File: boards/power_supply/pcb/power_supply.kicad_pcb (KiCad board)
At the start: 2 copper layers, 258 x 170 mm, 227 parts, among them J101 Battery, J102 5V, J103 3.3V, J104 V_ISOLATED, J201 Conn_01x04_Socket, J202 12401826E412A, J203 USB IDC, J301 Conn_01x02_Socket, J302 Conn_01x04_Socket, SW201 PTS526 SK15 SMTR2 LFS, T701 150u, U201 USBLC6-2P6

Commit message: initial psu charger layout
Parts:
- J101: footprint Connector_AMASS:AMASS_XT30U-F_1x02_P5.0mm_Vertical -> xt30:AMASS_XT30U-F_1x02_P5.0mm_Vertical
- J102, J103, J104, J301: footprint Connector_PinHeader_2.54mm:PinHeader_1x02_P2.54mm_Vertical -> Connector_JST:JST_XH_B2B-XH-A_1x02_P2.50mm_Vertical
- J202: value 12401826E412A -> USB4105-GF-A; footprint 12401826E412A:12401826E412A -> USB4105-GF-A:USB4105-GF-A
- J302: footprint Connector_PinHeader_2.54mm:PinHeader_1x04_P2.54mm_Vertical -> Connector_JST:JST_XH_B4B-XH-A_1x04_P2.50mm_Vertical
- moved JP301 73.1 mm to (106.9, 155.2), turned to 90 degrees
- moved R304 72.3 mm to (104.4, 152.1), turned to -90 degrees
- moved JP304 70.6 mm to (91.9, 155.2), turned to 90 degrees
- moved JP305 68.2 mm to (104.4, 155.2), turned to 90 degrees
- moved JP302 68.0 mm to (99.4, 155.2), turned to 90 degrees
- moved R305 67.7 mm to (96.9, 152.1), turned to -90 degrees
- moved JP308 67.3 mm to (101.9, 155.2), turned to 90 degrees
- moved J301 66.2 mm to (85.0, 150.4), turned to 90 degrees
- moved R301 65.8 mm to (106.9, 152.1), turned to -90 degrees
- moved R307 64.4 mm to (101.9, 152.1), turned to -90 degrees
- moved JP310 64.3 mm to (99.4, 148.9), turned to 90 degrees
- moved JP307 64.3 mm to (96.9, 148.9), turned to 90 degrees
- moved JP306 63.7 mm to (96.9, 155.2), turned to 90 degrees
- moved R214 63.6 mm to (111.1, 154.5), turned to -90 degrees
- moved JP309 63.5 mm to (94.4, 155.2), turned to 90 degrees
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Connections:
- D201 pad 2: /USB-C PD/VBUS -> VBUS
- D205 pad 2: /USB-C PD/VBUS -> VBUS
- J101 pad 1: /Charger/VBATT -> GND
- J101 pad 2: GND -> /Charger/VBATT
- R206 pad 1: /USB-C PD/VBUS -> VBUS
- U203 pad 5: /USB-C PD/VBUS -> VBUS
- U203 pad 6: /USB-C PD/VBUS -> VBUS
- U203 pad 7: /USB-C PD/VBUS -> VBUS
- U203 pad 8: /USB-C PD/VBUS -> VBUS
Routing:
- net /Charger/ILIM: track 0.00 -> 31.0 mm, vias 0 -> 2
- net VBUS: track 0.00 -> 25.9 mm
- net /Charger/CELL: track 0.00 -> 19.0 mm, vias 0 -> 2
- net /USB-C PD/CC1: track 0.00 -> 18.2 mm
- net /USB-C PD/CC2: track 0.00 -> 17.8 mm
- net /Charger/NTC: track 0.00 -> 17.8 mm, vias 0 -> 2
- net /Charger/ISET: track 0.00 -> 15.9 mm, vias 0 -> 2
- net /Charger/VB: track 0.00 -> 15.5 mm, vias 0 -> 2
- net /USB-C PD/ADDR1: track 0.00 -> 12.4 mm
- net /USB-C PD/ADDR0: track 0.00 -> 11.1 mm
- net Net-(U301-VCC): track 0.00 -> 9.58 mm, vias 0 -> 2
- net Net-(U301-CSP): track 0.00 -> 9.36 mm, vias 0 -> 2
- net Net-(C202-Pad1): track 0.00 -> 8.00 mm
- net Net-(U301-BST): track 0.00 -> 7.61 mm, vias 0 -> 2
- net /Charger/VIN: track 0.00 -> 7.54 mm
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- added copper zone on F.Cu, net /Buck-Boost-1/VIN
- added copper zone on F.Cu, net /Charger/VBATT
- added copper zone on F.Cu, net /Charger/VIN
- added copper zone on In1.Cu, net GND
- added copper zone on In2.Cu, net GND
- added copper zone on F.Cu, net Net-(U301-BST)
- added copper zone on F.Cu, net Net-(U301-CSP)
- added copper zone on F.Cu, net Net-(U301-SW)
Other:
- board size 258 x 170 mm -> 121.8 x 143.8 mm
- copper layers 2 -> 4

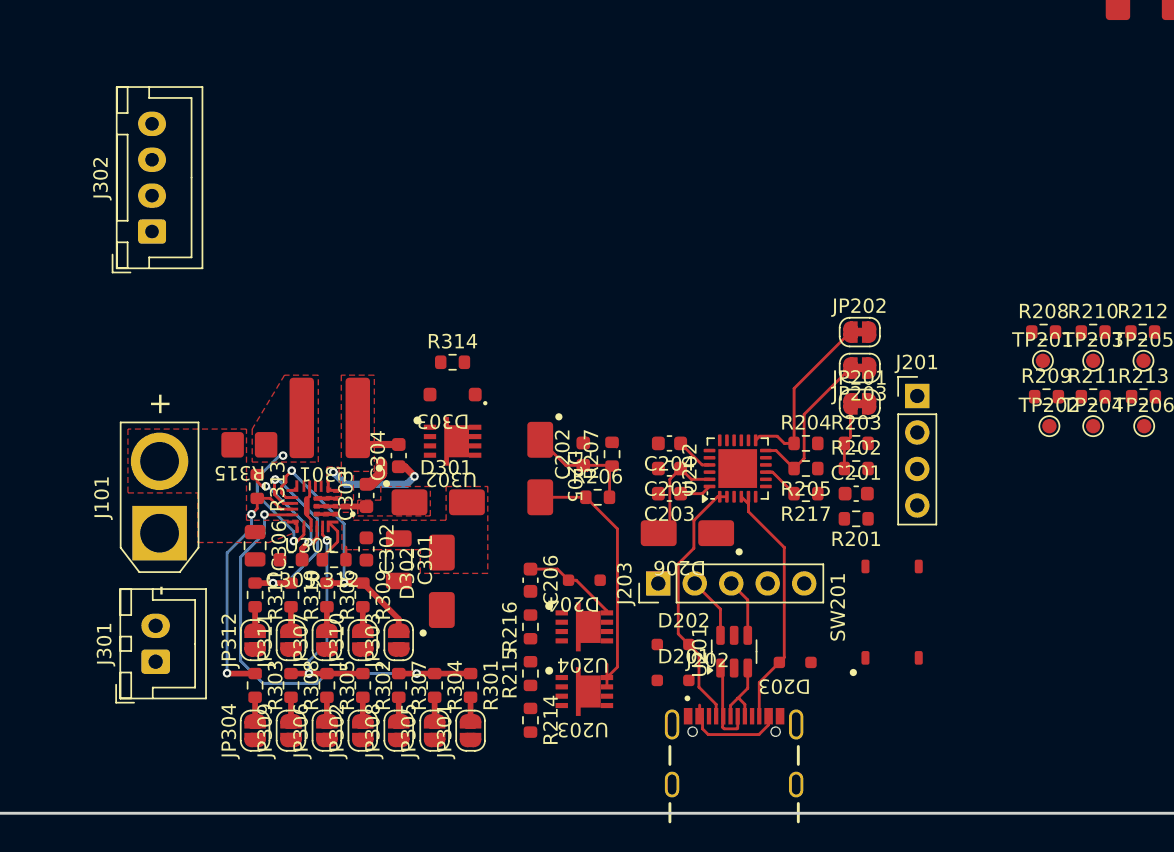
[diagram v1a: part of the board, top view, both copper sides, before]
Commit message: psu stusb4500 layouting
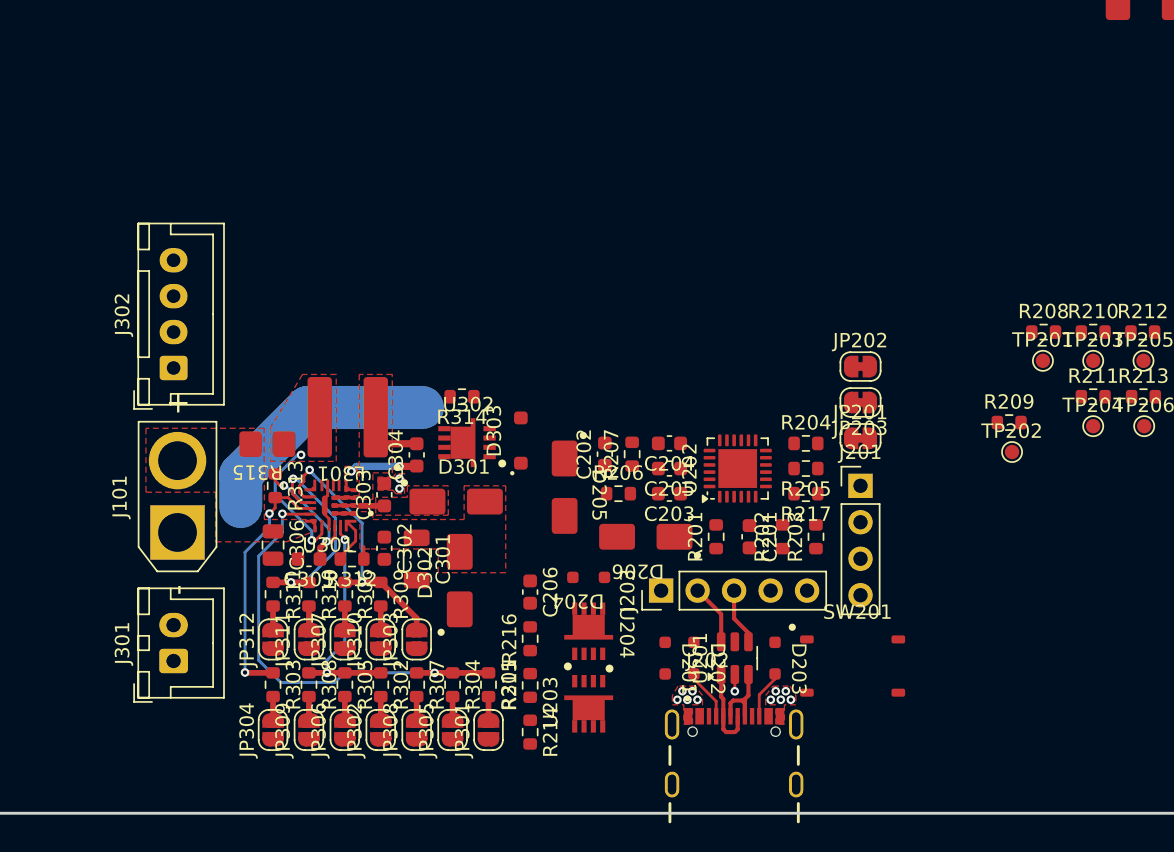
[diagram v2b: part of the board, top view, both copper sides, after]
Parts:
- moved R201 9.83 mm to (124.0, 141.8), turned to 90 degrees
- moved J302 9.62 mm to (86.2, 130.0)
- moved C201 8.02 mm to (126.3, 141.8), turned to -90 degrees
- moved J201 7.39 mm to (134.1, 138.2)
- moved R203 7.08 mm to (130.9, 141.8), turned to 90 degrees
- moved R202 6.98 mm to (128.6, 141.8), turned to 90 degrees
- moved D303 5.73 mm to (110.4, 135.1), turned to 90 degrees
- moved SW201 4.65 mm to (133.5, 150.8), turned to 0 degrees
- moved R209 3.16 mm to (144.4, 133.8)
- moved TP202 3.16 mm to (144.6, 135.8)
- moved D206 2.91 mm to (119.1, 141.8)
- moved R314 2.49 mm to (106.3, 132.0), turned to 180 degrees
- moved JP201 2.40 mm to (134.1, 134.9)
- moved JP202 2.40 mm to (134.1, 129.9)
- moved JP203 2.40 mm to (134.1, 132.4)
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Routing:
- net VBUS: track 25.9 -> 0.00 mm
- net (no net): track 0.00 -> 16.8 mm
- net /USB-C PD/CC1: track 18.2 -> 3.59 mm
- net /USB-C PD/CC2: track 17.8 -> 3.40 mm
- net /USB-C PD/ADDR1: track 12.4 -> 0.00 mm
- net /USB-C PD/ADDR0: track 11.1 -> 0.00 mm
- net Net-(C202-Pad1): track 8.00 -> 0.00 mm
- net Net-(U202-VREG_2V7): track 7.45 -> 0.00 mm
- net /Charger/VIN: track 7.54 -> 0.88 mm
- net Net-(JP201-A): track 4.68 -> 0.00 mm
- net Net-(U301-BST): track 7.61 -> 4.71 mm
- net Net-(U202-VREG_1V2): track 2.63 -> 0.00 mm
- net Net-(U202-DISCH): track 2.58 -> 0.00 mm
- net Net-(U202-VDD): track 2.22 -> 0.00 mm
- net GND: track 5.07 -> 4.22 mm, vias 0 -> 13
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- added copper zone on F.Cu, net GND

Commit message: psu layouting
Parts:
- moved C622 74.7 mm to (114.3, 126.5), turned to 90 degrees
- moved R101 58.3 mm to (141.6, 149.2)
- moved R102 58.3 mm to (141.6, 151.7)
- moved R103 58.3 mm to (141.6, 154.2)
- moved T701 56.9 mm to (142.2, 105.3)
- moved C603 54.2 mm to (101.5, 121.6)
- moved C604 54.2 mm to (101.5, 124.7)
- moved C619 54.2 mm to (96.5, 122.2)
- moved C620 54.2 mm to (96.5, 125.5)
- moved JP601 54.2 mm to (105.9, 124.1)
- moved R610 54.2 mm to (106.4, 127.6)
- moved TP602 54.2 mm to (91.8, 124.0)
- moved C602 54.2 mm to (101.5, 118.6)
- moved C608 54.2 mm to (101.5, 127.7)
- moved C618 54.2 mm to (96.5, 118.8)
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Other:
- board size 121.8 x 143.8 mm -> 83.7 x 76.5 mm

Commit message: psu layouting
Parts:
- C201, C202, C206, C304, C601, C602, C603, C604, C605, C606, C607, C609, C612, C614, C616, C618, C619, C620, C621, C622, D204, D205, D206, D303, JP201, JP202, JP203, JP301, JP302, JP303, JP304, JP305, JP306, JP307, JP308, JP309, JP310, JP311, JP312, JP601, R201, R202, R203, R204, R205, R206, R207, R208, R209, R210, R211, R212, R213, R214, R215, R216, R301, R302, R303, R304, R305, R306, R307, R308, R309, R310, R311, R312, R313, R314, R601, R602, R603, R604, R605, R606, R611, TP201, TP202, TP203, TP204, TP205, TP206, TP601, TP602: moved to B.Cu
- C303: footprint Capacitor_SMD:C_0603_1608Metric -> Capacitor_SMD:C_1206_3216Metric
- moved R103 95.7 mm to (99.8, 68.1)
- moved R101 89.0 mm to (202.7, 84.4)
- moved TP602 77.5 mm to (109.8, 48.6), turned to 180 degrees
- moved JP601 75.4 mm to (105.0, 48.7), turned to 180 degrees
- moved TP601 74.1 mm to (107.7, 48.7), turned to 180 degrees
- moved T701 67.1 mm to (195.2, 64.2)
- moved D702 67.1 mm to (197.0, 74.2)
- moved C706 66.8 mm to (208.3, 73.7)
- moved C701 66.8 mm to (208.3, 70.4)
- moved JP701 66.8 mm to (191.9, 74.5)
- moved JP702 66.8 mm to (191.9, 78.0)
- moved C703 66.8 mm to (203.4, 60.3)
- moved C705 66.8 mm to (196.3, 77.3)
- moved R701 66.8 mm to (203.4, 65.3)
- moved R704 66.8 mm to (203.4, 72.9)
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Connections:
- J202 pad SH1: SHIELD -> SHIELD_2
- J202 pad SH3: SHIELD_2 -> SHIELD_3
- J202 pad SH4: SHIELD_3 -> SHIELD
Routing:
- net /Charger/ILIM: track 31.0 -> 1.20 mm, vias 2 -> 1
- net /Charger/CELL: track 19.0 -> 1.24 mm, vias 2 -> 1
- net (no net): track 16.8 -> 0.00 mm
- net /Charger/NTC: track 17.8 -> 1.23 mm, vias 2 -> 1
- net /Charger/VBATT: track 0.00 -> 16.2 mm
- net /Charger/ISET: track 15.9 -> 1.27 mm, vias 2 -> 1
- net /Charger/VB: track 15.5 -> 1.23 mm, vias 2 -> 1
- net Net-(U202-VBUS_EN_SNK): track 0.00 -> 11.3 mm
- net /USB-C PD/CC1: track 3.59 -> 14.9 mm
- net /USB-C PD/CC2: track 3.40 -> 12.7 mm
- net Net-(U301-CSP): track 9.36 -> 1.37 mm, vias 2 -> 1
- net Net-(R214-Pad1): track 0.00 -> 7.82 mm, vias 0 -> 2
- net Net-(U301-VCC): track 9.58 -> 2.49 mm, vias 2 -> 0
- net /Charger/VIN: track 0.88 -> 6.26 mm, vias 0 -> 1
- net Net-(D302-Pad1): track 0.00 -> 5.39 mm, vias 0 -> 1
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- added copper zone on F.Cu, net /Charger/EN
- added copper zone on F.Cu, net /Charger/~{ACOK}
- added copper zone on F.Cu, net Net-(U202-VDD)
- added copper zone on F.Cu, net VBUS
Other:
- board size 83.7 x 76.5 mm -> 50 x 50 mm

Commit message: psu layouting
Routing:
- net GND: track 8.18 -> 14.6 mm, vias 14 -> 24
- net Net-(U202-VBUS_EN_SNK): track 11.3 -> 12.7 mm
- net VBUS: vias 2 -> 4

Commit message: psu layout
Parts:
- removed R208, R209, R210, R211, R212, R213: 100k, Resistor_SMD:R_0603_1608Metric
- removed TP201, TP202, TP203, TP204, TP205, TP206: TestPoint, TestPoint:TestPoint_Pad_D1.0mm
- R202, R203: moved to F.Cu
- moved JP203 62.6 mm to (129.6, 115.2), turned to 90 degrees
- moved R202 60.0 mm to (130.8, 115.8)
- moved JP202 58.7 mm to (132.1, 115.2), turned to -90 degrees
- moved R205 55.6 mm to (130.6, 112.1), turned to -90 degrees
- moved R204 52.6 mm to (132.6, 112.1), turned to 90 degrees
- moved JP201 51.6 mm to (133.1, 118.7), turned to -90 degrees
- moved R201 51.2 mm to (132.7, 122.0)
- moved R203 48.7 mm to (130.8, 114.2)
- moved C201 40.8 mm to (132.7, 123.5), turned to 0 degrees
- moved JP301 37.1 mm to (95.0, 141.2)
- moved JP305 37.1 mm to (92.5, 141.2)
- moved R301 37.1 mm to (95.0, 144.3)
- moved R304 37.1 mm to (92.5, 144.3)
- moved JP308 37.1 mm to (90.0, 141.2)
- moved R307 37.1 mm to (90.1, 144.3)
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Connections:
- U202 pad 11: /USB-C PD/ATTACH -> unconnected-(U202-ATTACH-Pad11)
- U202 pad 14: /USB-C PD/POWER_OK3 -> unconnected-(U202-POWER_OK3-Pad14)
- U202 pad 15: /USB-C PD/GPIO -> unconnected-(U202-GPIO-Pad15)
- U202 pad 17: /USB-C PD/A_B_SIDE -> unconnected-(U202-A_B_SIDE-Pad17)
- U202 pad 19: /USB-C PD/ALERT -> unconnected-(U202-ALERT-Pad19)
- U202 pad 20: /USB-C PD/POWER_OK2 -> unconnected-(U202-POWER_OK2-Pad20)
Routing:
- net /USB-C PD/VSYS: track 1.22 -> 37.0 mm, vias 1 -> 2
- net /USB-C PD/RESET: track 1.30 -> 18.2 mm, vias 1 -> 2
- net GND: track 14.6 -> 28.1 mm, vias 24 -> 30
- net Net-(C202-Pad1): track 0.00 -> 9.81 mm
- net /USB-C PD/ADDR1: track 0.00 -> 8.92 mm, vias 0 -> 1
- net /USB-C PD/SCL: track 0.00 -> 8.91 mm
- net /USB-C PD/SDA: track 0.00 -> 8.58 mm
- net Net-(JP201-A): track 0.00 -> 7.66 mm, vias 0 -> 2
- net Net-(U202-VREG_2V7): track 2.55 -> 8.99 mm, vias 0 -> 1
- net /USB-C PD/ADDR0: track 0.00 -> 6.09 mm, vias 0 -> 1
- net Net-(U202-VBUS_VS_DISCH): track 0.00 -> 5.62 mm, vias 0 -> 1
- net Net-(U202-VBUS_EN_SNK): track 12.7 -> 17.1 mm, vias 0 -> 1
- net Net-(U202-DISCH): track 0.00 -> 3.61 mm
- net VBUS: track 0.00 -> 2.98 mm, vias 4 -> 2
- net /USB-C PD/ALERT: track 1.54 -> 0.00 mm, vias 1 -> 0
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- added copper zone on B.Cu, net /Charger/VBATT
- added copper zone on B.Cu, net VBUS

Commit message: psu layout
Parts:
- removed R214: 22k, Resistor_SMD:R_0603_1608Metric
- removed R215: 100k, Resistor_SMD:R_0603_1608Metric
- removed R216: 100, Resistor_SMD:R_0603_1608Metric
- removed R217: 1k, Resistor_SMD:R_0603_1608Metric
- added R208: 22k, Resistor_SMD:R_0603_1608Metric, B.Cu at (117.0, 122.7)
- added R209: 100k, Resistor_SMD:R_0603_1608Metric, B.Cu at (117.0, 124.2)
- added R210: 100, Resistor_SMD:R_0603_1608Metric, B.Cu at (117.0, 125.8)
- added R211: 1k, Resistor_SMD:R_0603_1608Metric, F.Cu at (130.8, 112.7)
- R312: moved to F.Cu
- moved T701 73.0 mm to (130.3, 97.5), turned to 180 degrees
- moved R311 33.6 mm to (108.3, 115.5), turned to 90 degrees
- moved R310 33.3 mm to (105.8, 115.5), turned to 90 degrees
- moved R103 31.3 mm to (101.7, 99.4), turned to -90 degrees
- moved C605 30.2 mm to (107.1, 73.3), turned to 90 degrees
- moved R309 29.9 mm to (103.2, 115.5), turned to 90 degrees
- moved R306 29.7 mm to (100.7, 115.5), turned to 90 degrees
- moved C608 29.2 mm to (103.9, 99.2), turned to 90 degrees
- moved JP303 29.2 mm to (98.1, 112.2), turned to -90 degrees
- moved C610 28.8 mm to (113.2, 102.5), turned to 90 degrees
- moved JP312 28.7 mm to (108.3, 112.2), turned to -90 degrees
- moved L601 28.5 mm to (109.0, 105.8)
- moved R607 28.4 mm to (103.5, 95.7), turned to 90 degrees
- moved C606 27.5 mm to (105.6, 73.3), turned to 90 degrees
- moved U601 27.5 mm to (109.0, 99.1), turned to 180 degrees
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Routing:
- net /Charger/NTC: track 1.23 -> 58.9 mm
- net /Charger/VIN: track 6.26 -> 49.0 mm, vias 1 -> 2
- net /Charger/EN: track 0.97 -> 41.7 mm
- net GND: track 28.1 -> 53.2 mm, vias 30 -> 34
- net /Charger/~{ACOK}: track 1.31 -> 23.2 mm
- net /Charger/VB: track 1.23 -> 21.3 mm
- net /Charger/CELL: track 1.24 -> 19.4 mm
- net /Charger/~{STAT}: track 1.37 -> 17.1 mm
- net Net-(U301-CSP): track 1.37 -> 16.9 mm, vias 1 -> 2
- net /Charger/ISET: track 1.27 -> 14.1 mm
- net Net-(U601-VOUT): track 0.00 -> 10.8 mm
- net Net-(U601-SW2): track 0.00 -> 10.7 mm
- net Net-(U601-SW1): track 0.00 -> 10.4 mm
- net /Buck-Boost-3/VOUT: track 0.00 -> 8.18 mm
- net /Charger/ILIM: track 1.20 -> 8.58 mm
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- added copper zone on B.Cu, net /Buck-Boost-1/VIN
